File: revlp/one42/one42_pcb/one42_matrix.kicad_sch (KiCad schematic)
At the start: 84 parts

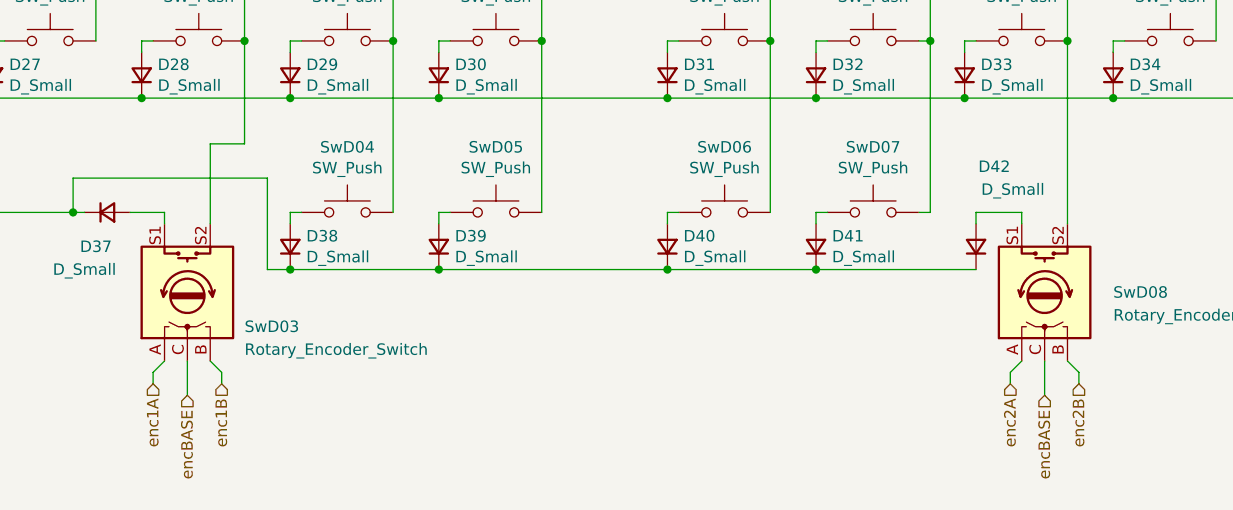
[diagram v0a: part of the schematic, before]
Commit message: [project] One42: Update schematic & PDF
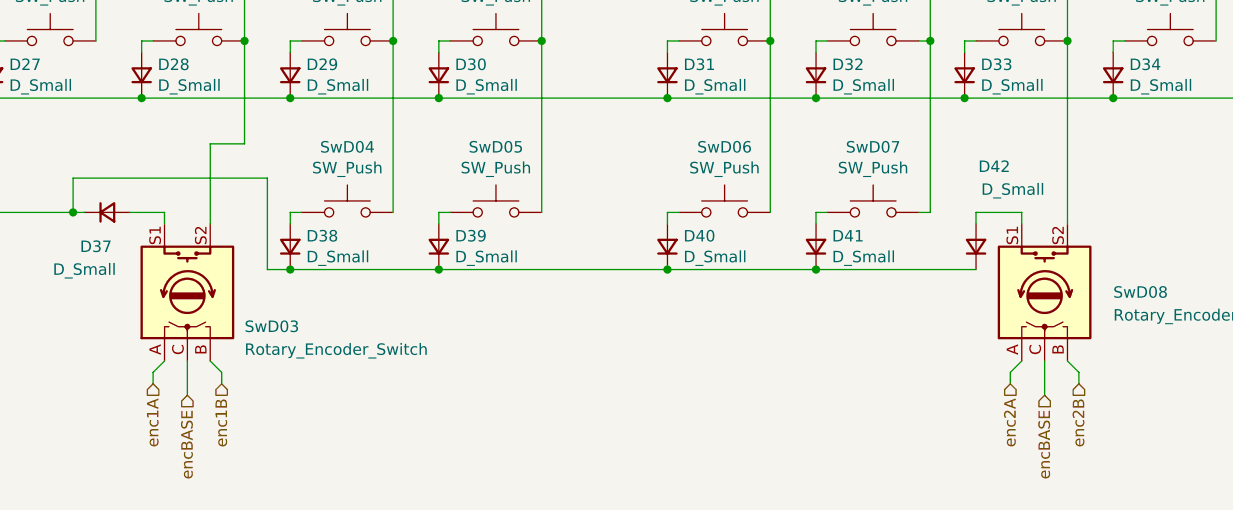
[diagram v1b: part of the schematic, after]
